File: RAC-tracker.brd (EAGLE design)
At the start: 26.9 x 62.2 mm, 24 parts, among them J3 47346-1001, U2 SIM-ST-MFF2, U3 MCP73831, U4 SKY65723-81

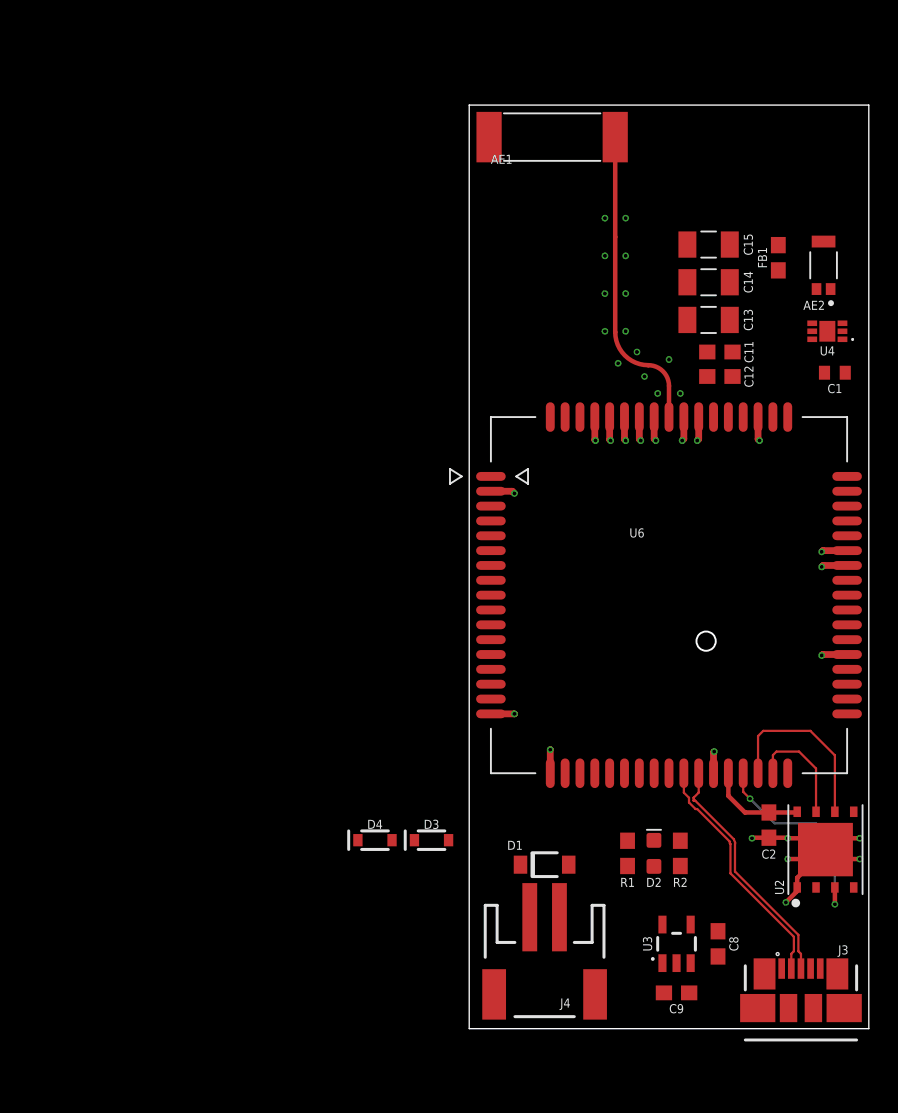
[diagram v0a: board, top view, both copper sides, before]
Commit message: Added ATMEGA328P and BMP388 to schematic, likely won't keep
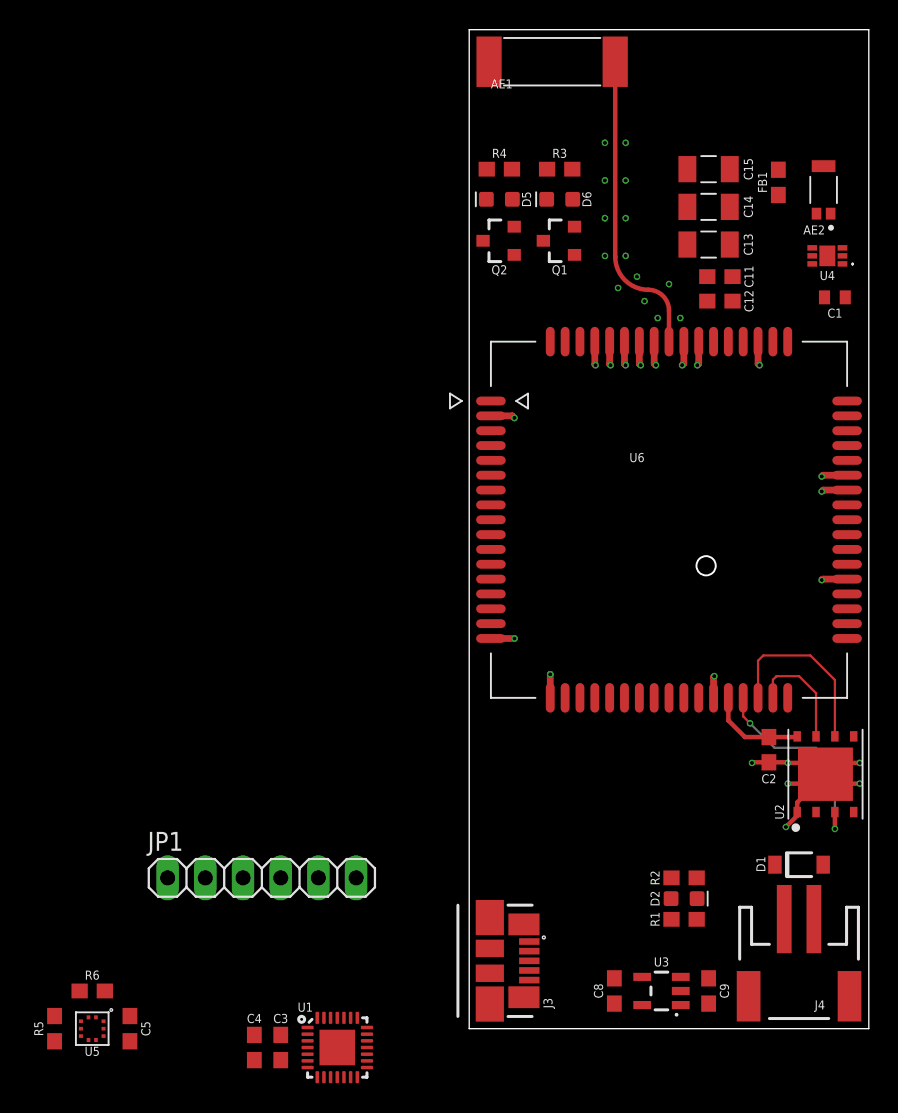
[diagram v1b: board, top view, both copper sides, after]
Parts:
- removed D3, D4: 250mA/100V, SparkFun-DiscreteSemi:SOD-323
- added C3, C5: 0.1uF, SparkFun-Capacitors:0603
- added C4: 4.7uF, SparkFun-Capacitors:0603
- added D5: BLUE, SparkFun-LED:LED-0603
- added D6: GREEN, SparkFun-LED:LED-0603
- added JP1: (no value), pinhead:1X06
- added Q1, Q2: 220mA/50V/3.5Ω, SparkFun-DiscreteSemi:SOT23-3
- added R3: 2.0k, SparkFun-Resistors:0603
- added R4: 470, SparkFun-Resistors:0603
- added R5, R6: 4.7k, SparkFun-Resistors:0603
- added U1: ATMEGA328P, SparkFun-IC-Microcontroller:VQFN-28
- added U5: BMP388, SparkFun-Sensors:LGA-10(2X2)
- moved J3 23.7 mm to (-0.76, 4.57), turned to 90 degrees
- moved J4 17.1 mm to (22.2, 3.68)
- moved D1 17.1 mm to (22.2, 11.0)
- moved C8 7.67 mm to (9.78, 2.54)
- moved R1 5.85 mm to (14.5, 7.37), turned to 180 degrees
- moved C1 5.08 mm to (24.6, 49.3)
- moved FB1 5.08 mm to (20.8, 57.0)
- moved C2 5.08 mm to (20.2, 18.8)
- moved U2 5.08 mm to (24.0, 17.1)
- moved AE1 5.08 mm to (5.59, 65.2)
- moved AE2 5.08 mm to (23.9, 56.5)
- moved C11 5.08 mm to (16.9, 50.7)
- moved C12 5.08 mm to (16.9, 49.0)
- moved C13 5.08 mm to (16.1, 52.8)
- moved C14 5.08 mm to (16.1, 55.4)
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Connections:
- removed net !LTE_RST: D4.C
- removed net LTE_PWR: D3.C
- removed net RXD: U6.10
- removed net TXD: U6.9
- new net LED_NET_A: D5.A, R4.1
- new net LED_NET_C: D5.C, Q2.3
- new net LED_STAT_A: D6.A, R3.1
- new net LED_STAT_C: D6.C, Q1.3
- new net LTE_RXD: U1.27, U6.10
- new net LTE_TXD: U1.26, U6.9
- new net MCU_RST: JP1.3, U1.25
- new net MISO: JP1.5, U1.14
- new net MOSI: JP1.4, U1.13
- new net NETLIGHT: Q2.1, U6.52
- new net SCK: JP1.6, U1.15
- new net SCL: R6.1, U1.24, U5.2
- new net SDA: R5.1, U1.23, U5.4
- new net STATUS: Q1.1, U6.66
- net 1.8V: now also C5.1, R5.2, R6.2, U5.1, U5.10, U5.6
- net DTR: now also U1.1
- net GND: now also C3.2, C4.2, C5.2, JP1.2, Q1.2, Q2.2, U1.18, U1.4, U1.PAD, U5.3, U5.8, U5.9
- net NRESET: now also U1.20; no longer D4.A
- net PWRKEY: now also U1.19; no longer D3.A
- net RI: now also U1.28
- net V_BATT: now also C3.1, C4.1, JP1.1, R3.2, R4.2, U1.16, U1.17, U1.3
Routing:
- net USB_P: track 16.4 -> 0.00 mm
- net USB_N: track 16.4 -> 0.00 mm
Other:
- board size 26.9 x 62.2 mm -> 26.9 x 67.3 mm
